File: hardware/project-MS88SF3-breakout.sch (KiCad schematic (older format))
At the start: 27 parts, among them J1 Conn_02x05_Odd_Even, J2 S2B-PH-SM4-TB(LF)(SN), J3 USB4105-GF-A, J4 Conn_01x12_Male, J5 Conn_01x16_Male, U1 MS88SF3_NRF52840

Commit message: Routing done
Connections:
- net NFC1: now also J5.2 (Pin_2); no longer J5.1 (Pin_1)
- net NFC2: now also J5.3 (Pin_3); no longer J5.2 (Pin_2)
- net P0.13: now also J5.9 (Pin_9); no longer J5.11 (Pin_11)
- net P0.17: now also J5.11 (Pin_11); no longer J5.9 (Pin_9)
- net P0.19: now also J5.8 (Pin_8); no longer J5.12 (Pin_12)
- net P0.21: now also J5.12 (Pin_12); no longer J5.8 (Pin_8)
- net P0.22: now also J5.5 (Pin_5); no longer J5.6 (Pin_6)
- net P0.25: now also J5.1 (Pin_1); no longer J5.5 (Pin_5)
- net RX: now also J5.4 (Pin_4); no longer J5.3 (Pin_3)
- net TX: now also J5.6 (Pin_6); no longer J5.4 (Pin_4)
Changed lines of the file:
@@
 Wire Wire Line
 	6200 4050 5850 4050
+Text Label 5850 3350 0    50   ~ 0
+TX
 Text Label 5850 3150 0    50   ~ 0
-TX
-Text Label 5850 3050 0    50   ~ 0
 RX
 Wire Wire Line
-	6200 3050 5850 3050
-Wire Wire Line
 	6200 3150 5850 3150
+Wire Wire Line
+	6200 3350 5850 3350
 Text Label 4900 2850 0    50   ~ 0
 P1.10
@@
 Wire Wire Line
 	4900 3450 5250 3450
-Text Label 5850 3250 0    50   ~ 0
-P0.25
-Wire Wire Line
-	5850 3250 6200 3250
+Text Label 5850 3050 0    50   ~ 0
+NFC2
+Wire Wire Line
+	5850 3050 6200 3050
 Text Label 5850 2950 0    50   ~ 0
-NFC2
+NFC1
 Wire Wire Line
 	5850 2950 6200 2950
-Text Label 5850 3350 0    50   ~ 0
-P0.22
-Wire Wire Line
-	5850 3350 6200 3350
-Text Label 5850 3450 0    50   ~ 0
-P0.23
-Wire Wire Line
-	5850 3450 6200 3450
-Text Label 5850 3550 0    50   ~ 0
-P0.21
-Wire Wire Line
-	5850 3550 6200 3550
-Text Label 5850 3650 0    50   ~ 0
-P0.17
-Wire Wire Line
-	5850 3650 6200 3650
-Text Label 5850 3750 0    50   ~ 0
-P0.15
-Wire Wire Line
-	5850 3750 6200 3750
-Text Label 5850 3850 0    50   ~ 0
-P0.13
-Wire Wire Line
-	5850 3850 6200 3850
-Text Label 5850 3950 0    50   ~ 0
-P0.19
-Wire Wire Line
-	5850 3950 6200 3950
-Text Label 5850 2850 0    50   ~ 0
-NFC1
-Wire Wire Line
-	5850 2850 6200 2850
 Wire Wire Line
 	4250 4050 3900 4050
@@
 Wire Wire Line
 	1150 2450 1500 2450
+Wire Wire Line
+	5850 3550 6200 3550
+Text Label 5850 3550 0    50   ~ 0
+P0.19
+Wire Wire Line
+	5850 3650 6200 3650
+Text Label 5850 3650 0    50   ~ 0
+P0.13
+Wire Wire Line
+	5850 3750 6200 3750
+Text Label 5850 3750 0    50   ~ 0
+P0.15
+Wire Wire Line
+	5850 3850 6200 3850
+Text Label 5850 3850 0    50   ~ 0
+P0.17
+Wire Wire Line
+	5850 3950 6200 3950
+Text Label 5850 3950 0    50   ~ 0
+P0.21
+Wire Wire Line
+	5850 3450 6200 3450
+Text Label 5850 3450 0    50   ~ 0
+P0.23
+Wire Wire Line
+	5850 3250 6200 3250
+Text Label 5850 3250 0    50   ~ 0
+P0.22
+Wire Wire Line
+	5850 2850 6200 2850
+Text Label 5850 2850 0    50   ~ 0
+P0.25
 $EndSCHEMATC

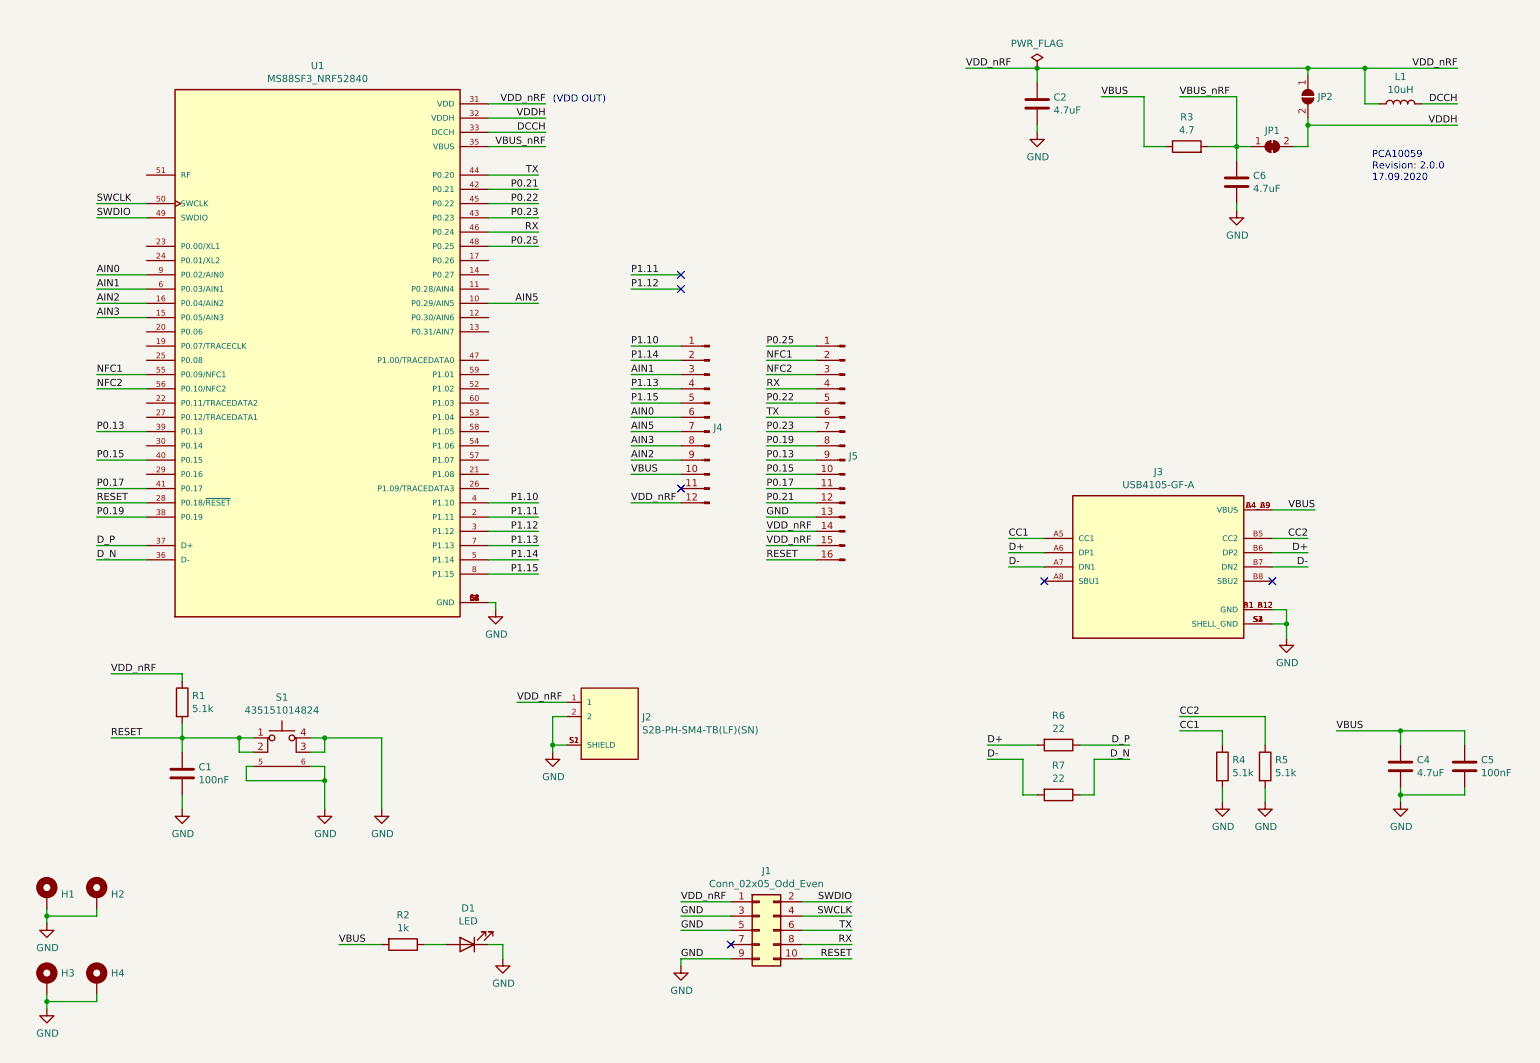
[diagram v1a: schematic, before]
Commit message: Clean up schematic
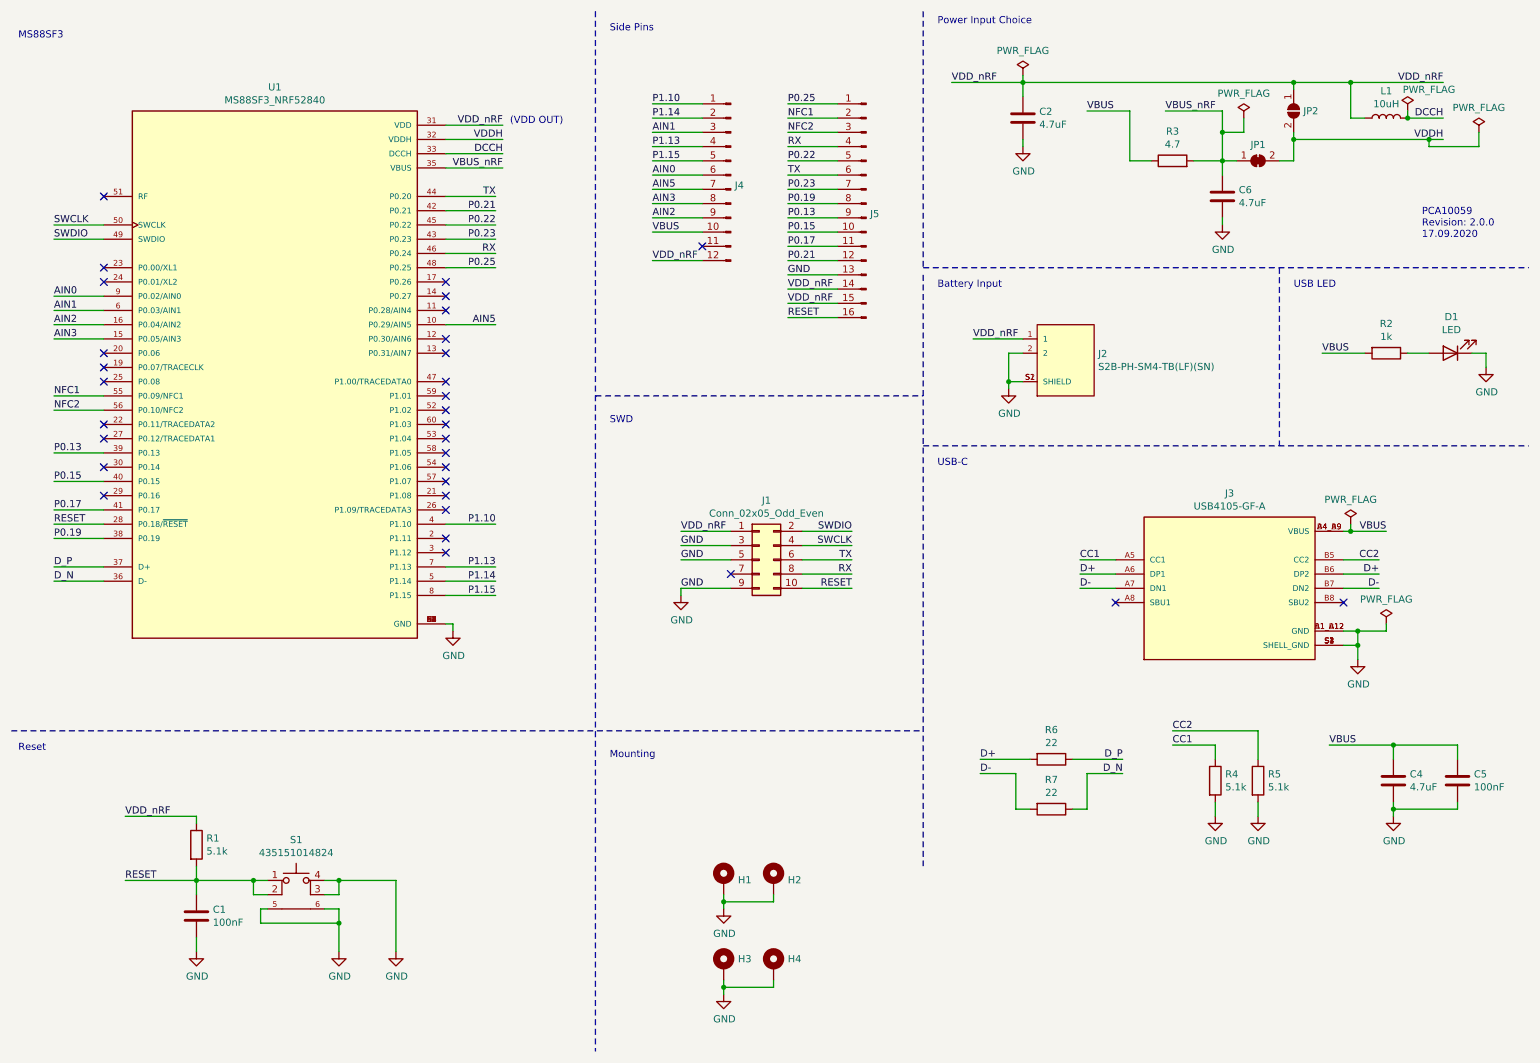
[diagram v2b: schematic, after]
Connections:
- net P1.11: no longer names the net of U1.2 (P1.11)
- net P1.12: no longer names the net of U1.3 (P1.12)
- no-connect marks 6 -> 31
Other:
- note added: "Battery Input"
- note added: "MS88SF3"
- note added: "Mounting"
- note added: "Power Input Choice"
- note added: "Reset"
- note added: "SWD"
- note added: "Side Pins"
- note added: "USB LED"
- note added: "USB-C"
- moved on the sheet: C1, C2, C4, C5, C6, D1, H1, H2, H3, H4, J1, J2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
